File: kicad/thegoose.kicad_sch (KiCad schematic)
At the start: 35 parts, among them U1 DRV8848, U2 DRV8848, U3 DRV8848, U4 AP64500SP-13

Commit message: Tie DRV8848 sense pins to GND
AISEN and BISEN on U1-U3 were left open, so the H-bridges' low side had
no return path. Without current limiting, the data sheet says to tie
them to GND. Done in the SKiDL source, the schematic and the PCB (short
tracks from each pad to GND).

The PCB file is now saved in KiCad 10 format, which accounts for most of
its diff.

Co-Authored-By: Claude Opus 5.5 <noreply@anthropic.com>
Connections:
- net GND: now also U1.3 (AISEN), U1.6 (BISEN), U2.3 (AISEN), U2.6 (BISEN), U3.3 (AISEN), U3.6 (BISEN)
- no-connect marks 16 -> 10

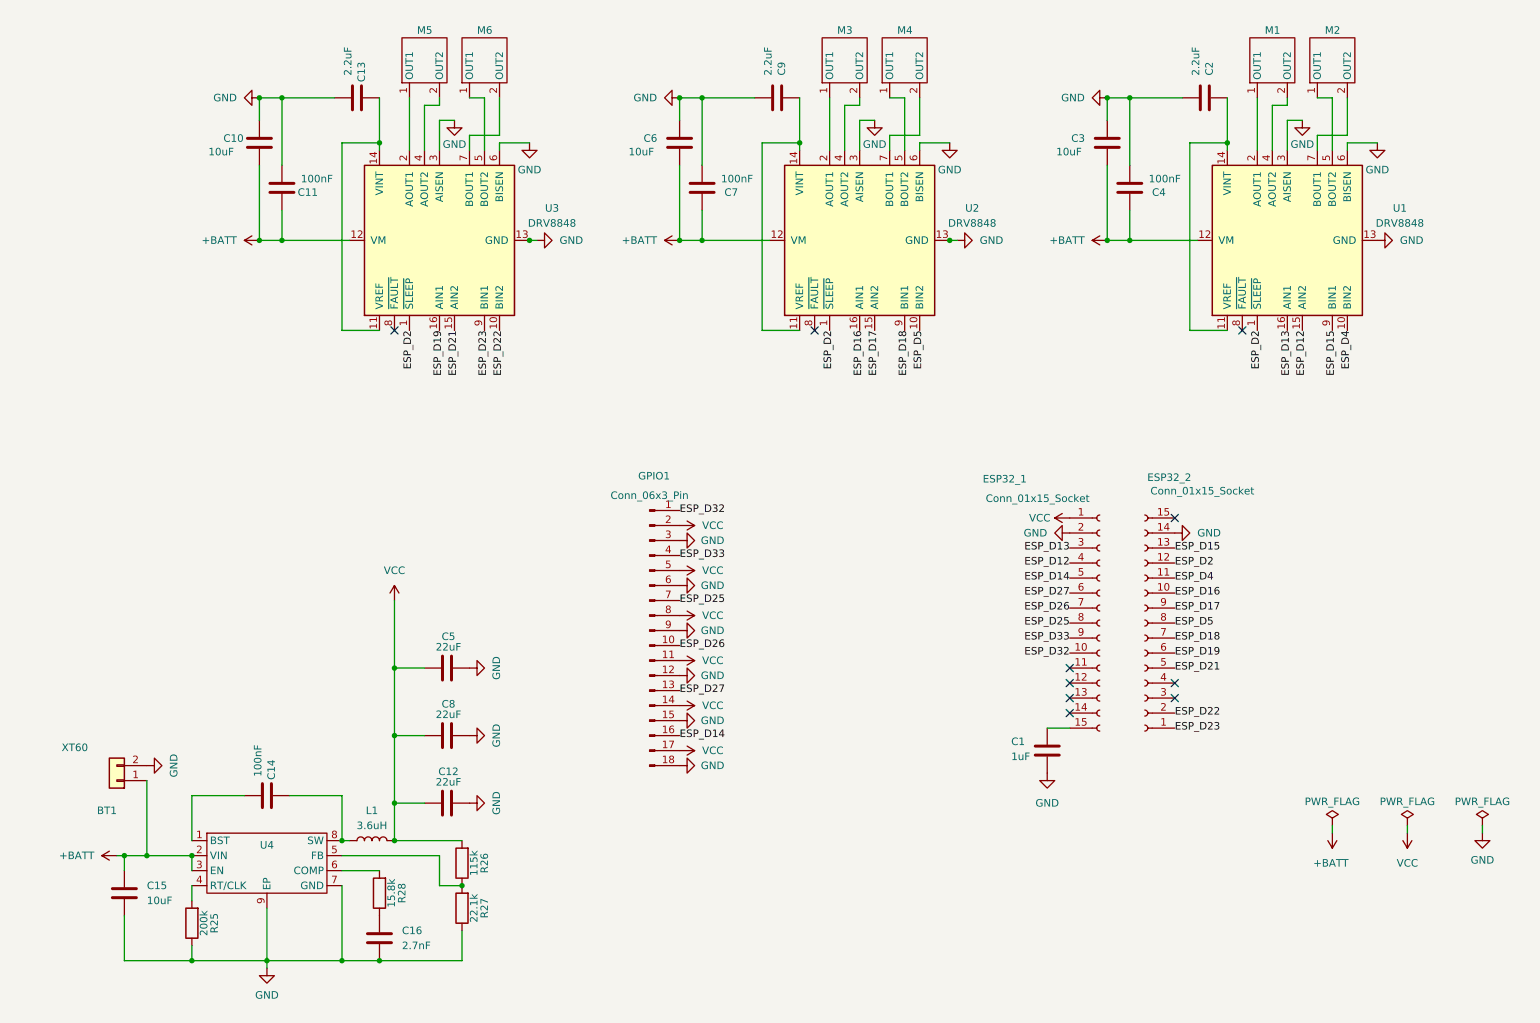
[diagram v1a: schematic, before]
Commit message: Tidy the schematic with the review loop
Six schematic-loop iterations raised the critic score from 2.9 to 4.3:
clearer power symbols, separated wiring, block titles and design notes.
Connectivity is unchanged (the netlist still matches SKiDL).

Co-Authored-By: Claude Opus 5.5 <noreply@anthropic.com>
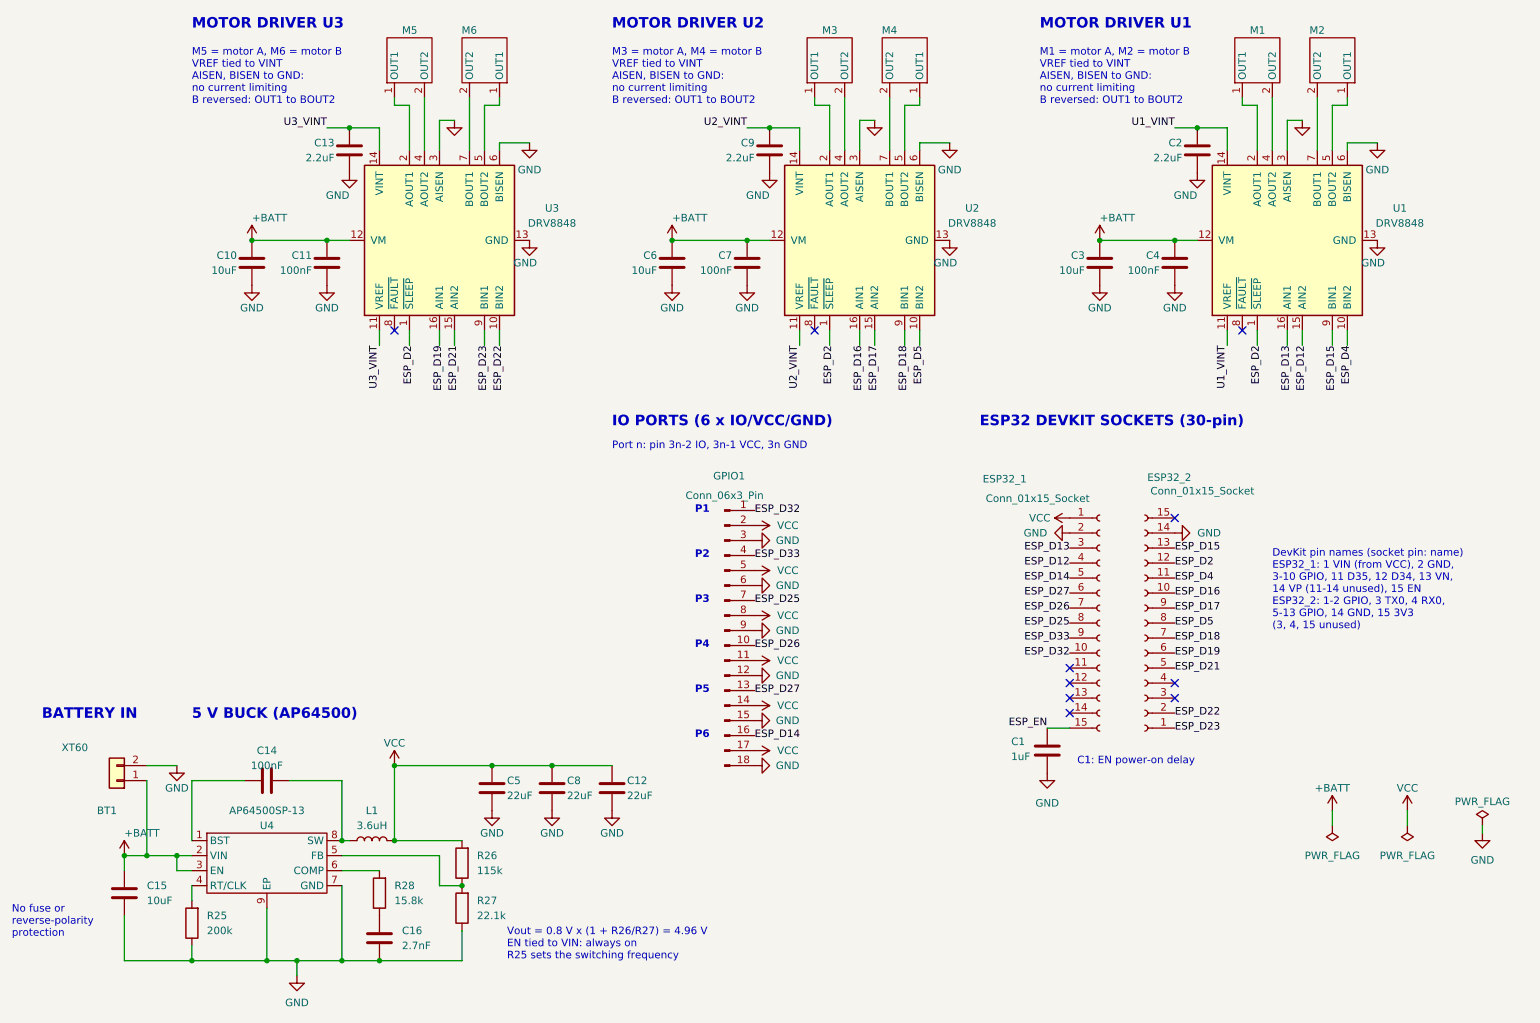
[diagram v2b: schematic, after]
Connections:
- net U1_VINT: now reaches C2.1, U1.11 (VREF), U1.14 (VINT)
- net ESP_EN: now reaches C1.1, ESP32_1.15 (Pin_15)
- net U3_VINT: now reaches C13.1, U3.11 (VREF), U3.14 (VINT)
- net U2_VINT: now reaches C9.1, U2.11 (VREF), U2.14 (VINT)
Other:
- note added: "5 V BUCK (AP64500)"
- note added: "BATTERY IN"
- note added: "C1: EN power-on delay"
- note added: "DevKit pin names (socket pin: name) ESP32_1: 1 VIN (from VCC), 2 GND, 3-10 GPIO, 11 D35, 12 D34, 13 VN, 14 VP (11-14 unused), 15 EN ESP32_2: 1-2 GPIO, 3 TX0, 4 RX0, 5-13 GPIO, 14 GND, 15 3V3 (3, 4, 15 unused)"
- note added: "ESP32 DEVKIT SOCKETS (30-pin)"
- note added: "IO PORTS (6 x IO/VCC/GND)"
- note added: "M1 = motor A, M2 = motor B VREF tied to VINT AISEN, BISEN to GND: no current limiting B reversed: OUT1 to BOUT2"
- note added: "M3 = motor A, M4 = motor B VREF tied to VINT AISEN, BISEN to GND: no current limiting B reversed: OUT1 to BOUT2"
- note added: "M5 = motor A, M6 = motor B VREF tied to VINT AISEN, BISEN to GND: no current limiting B reversed: OUT1 to BOUT2"
- note added: "MOTOR DRIVER U1"
- note added: "MOTOR DRIVER U2"
- note added: "MOTOR DRIVER U3"
- note added: "No fuse or reverse-polarity protection"
- note added: "P1"
- note added: "P2"
- note added: "P3"
- note added: "P4"
- note added: "P5"
- note added: "P6"
- note added: "Port n: pin 3n-2 IO, 3n-1 VCC, 3n GND"
- note added: "Vout = 0.8 V x (1 + R26/R27) = 4.96 V EN tied to VIN: always on R25 sets the switching frequency"
- moved on the sheet: C10, C11, C12, C13, C14, C2, C3, C4, C5, C6, C7, C8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

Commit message: Draw the rev 2 schematic as hierarchical sheets
Top sheet plus Power & charging, MCU & USB, Motor drivers and IO,
redrawn from circuit/goosebrain.py and tidied with the schematic loop.
ERC is clean and the netlist matches SKiDL, including MPN and LCSC.

- Add footprints for the Abracon AOTA core inductor and the Amphenol
  87520 USB-A receptacle.
- Fix L1's footprint name for KiCad 10's Wurth library.
- Keep battery sense on VSYS so it drains nothing with the switch off.
- Update the schematic critic's rubric for the rev 2 blocks.

Co-Authored-By: Claude Opus 5.5 <noreply@anthropic.com>
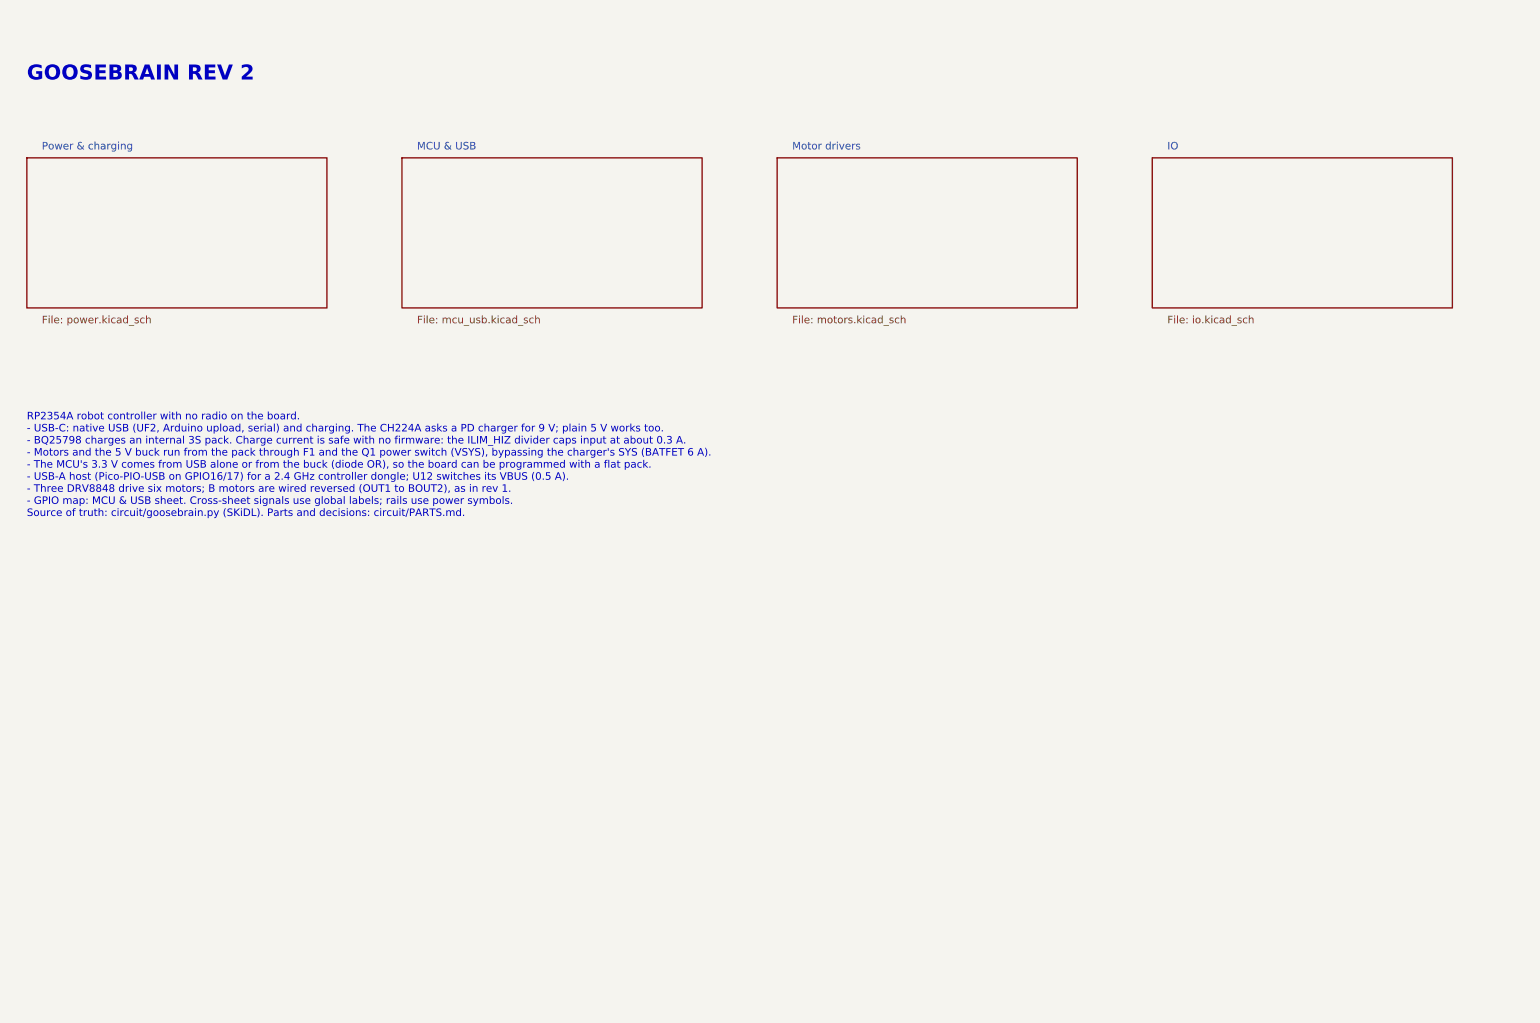
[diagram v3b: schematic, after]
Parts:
- removed BT1: XT60, hexy:AMASS_XT60PW-M_1x02_P7.20mm_Horizontal, symbol Connector_Generic:Conn_01x02
- removed C1: 1uF, Capacitor_SMD:C_0805_2012Metric, symbol Device:C
- removed C10, C15, C3, C6: 10uF, Capacitor_SMD:C_0805_2012Metric, symbol Device:C
- removed C11, C14, C4, C7: 100nF, Capacitor_SMD:C_0805_2012Metric, symbol Device:C
- removed C12, C5, C8: 22uF, Capacitor_SMD:C_0603_1608Metric, symbol Device:C
- removed C13, C2, C9: 2.2uF, Capacitor_SMD:C_0805_2012Metric, symbol Device:C
- removed C16: 2.7nF, Capacitor_SMD:C_0603_1608Metric, symbol Device:C
- removed ESP32_1, ESP32_2: Conn_01x15_Socket, Connector_PinSocket_2.54mm:PinSocket_1x15_P2.54mm_Vertical, symbol Connector:Conn_01x15_Socket
- removed GPIO1: Conn_06x3_Pin, hexy:PinHeader_3x06_P2.54mm_Horizontal, symbol Connector:Conn_01x18_Pin
- removed L1: 3.6uH, Inductor_SMD_Wurth:L_Wurth_WE-LQSH-4020, symbol Device:L
- removed M1, M2, M3, M4, M5, M6: ~, hexy:JST_XH_S2B-XH-A_1x02_P2.50mm_Horizontal, symbol hexyhustle:motor
- removed R25: 200k, Resistor_SMD:R_0805_2012Metric_Pad1.20x1.40mm_HandSolder, symbol Device:R
- removed R26: 115k, Resistor_SMD:R_0805_2012Metric_Pad1.20x1.40mm_HandSolder, symbol Device:R
- removed R27: 22.1k, Resistor_SMD:R_0805_2012Metric_Pad1.20x1.40mm_HandSolder, symbol Device:R
- removed R28: 15.8k, Resistor_SMD:R_0805_2012Metric_Pad1.20x1.40mm_HandSolder, symbol Device:R
- removed U1, U2, U3: DRV8848, Package_SO:TSSOP-16-1EP_4.4x5mm_P0.65mm, symbol Driver_Motor:DRV8848
- removed U4: AP64500SP-13, Package_SO:Diodes_SO-8EP, symbol hexyhustle:AP64500-13
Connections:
- no-connect marks 10 -> 0
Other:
- added sheet IO (io.kicad_sch)
- added sheet MCU & USB (mcu_usb.kicad_sch)
- added sheet Motor drivers (motors.kicad_sch)
- added sheet Power & charging (power.kicad_sch)
- note added: "GOOSEBRAIN REV 2"
- note added: "RP2354A robot controller with no radio on the board. - USB-C: native USB (UF2, Arduino upload, serial) and charging. The CH224A asks a PD charger for 9 V; plain 5 V works too. - BQ25798 charges an internal 3S pack. Charge current is safe with no firmware: the ILIM_HIZ divider caps input at about 0.3 A. - Motors and the 5 V buck run from the pack through F1 and the Q1 power switch (VSYS), bypassin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"
- note removed: "5 V BUCK (AP64500)"
- note removed: "BATTERY IN"
- note removed: "C1: EN power-on delay"
- note removed: "DevKit pin names (socket pin: name) ESP32_1: 1 VIN (from VCC), 2 GND, 3-10 GPIO, 11 D35, 12 D34, 13 VN, 14 VP (11-14 unused), 15 EN ESP32_2: 1-2 GPIO, 3 TX0, 4 RX0, 5-13 GPIO, 14 GND, 15 3V3 (3, 4, 15 unused)"
- note removed: "ESP32 DEVKIT SOCKETS (30-pin)"
- note removed: "IO PORTS (6 x IO/VCC/GND)"
- note removed: "M1 = motor A, M2 = motor B VREF tied to VINT AISEN, BISEN to GND: no current limiting B reversed: OUT1 to BOUT2"
- note removed: "M3 = motor A, M4 = motor B VREF tied to VINT AISEN, BISEN to GND: no current limiting B reversed: OUT1 to BOUT2"
- note removed: "M5 = motor A, M6 = motor B VREF tied to VINT AISEN, BISEN to GND: no current limiting B reversed: OUT1 to BOUT2"
- note removed: "MOTOR DRIVER U1"
- note removed: "MOTOR DRIVER U2"
- note removed: "MOTOR DRIVER U3"
- note removed: "No fuse or reverse-polarity protection"
- note removed: "P1"
- note removed: "P2"
- note removed: "P3"
- note removed: "P4"
- note removed: "P5"
- note removed: "P6"
- note removed: "Port n: pin 3n-2 IO, 3n-1 VCC, 3n GND"
- note removed: "Vout = 0.8 V x (1 + R26/R27) = 4.96 V EN tied to VIN: always on R25 sets the switching frequency"

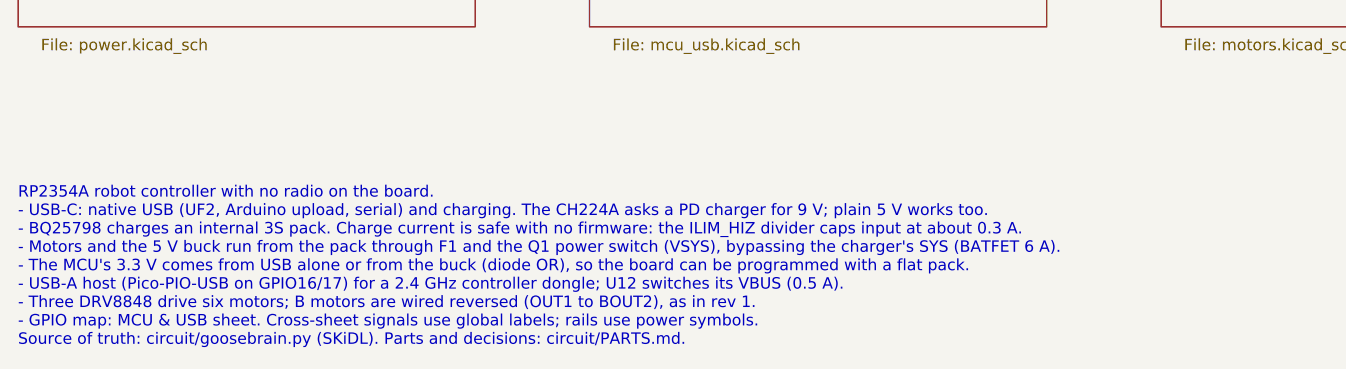
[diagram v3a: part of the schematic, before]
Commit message: Re-lay out rev 2 around an Ovonic 450 pack on top of the board
The internal pack is now an Ovonic 3S 450 mAh XT30 pack sitting 2 mm
above the board over the low-power logic area, on an XT30 pigtail. The
board is 88.5 x 47 mm with 2 mm corner radii, for a box of about
93.5 x 52 x 24.6 mm whose face has no openings.

- IO S1-S6 are a 3 x 6 right-angle header out of the left end, beside
  M5/M6, replacing the recessed vertical block.
- BOOT is a side-push switch on the top edge behind a pinhole sized for
  a 2.5 mm hex key; RESET is removed, with RUN on a bottom test pad
  beside SWCLK/SWDIO/GND.
- The CHG LED is a side-view part on the top edge; the GPIO status LED
  is removed now that the WS2812B stick shows status.
- The pack NTC is removed (a fixed 10k holds the charger's TS at 25 C);
  the protector's on-board TH1 stays.
- Q1, F1 and the other warm parts moved out from under the pack, and the
  GPIO map was re-swapped for the new placement (I2C on I2C1).

Schematic review passes; PCB review passes every gate except unrouted.

Co-Authored-By: Claude Opus 5.5 <noreply@anthropic.com>
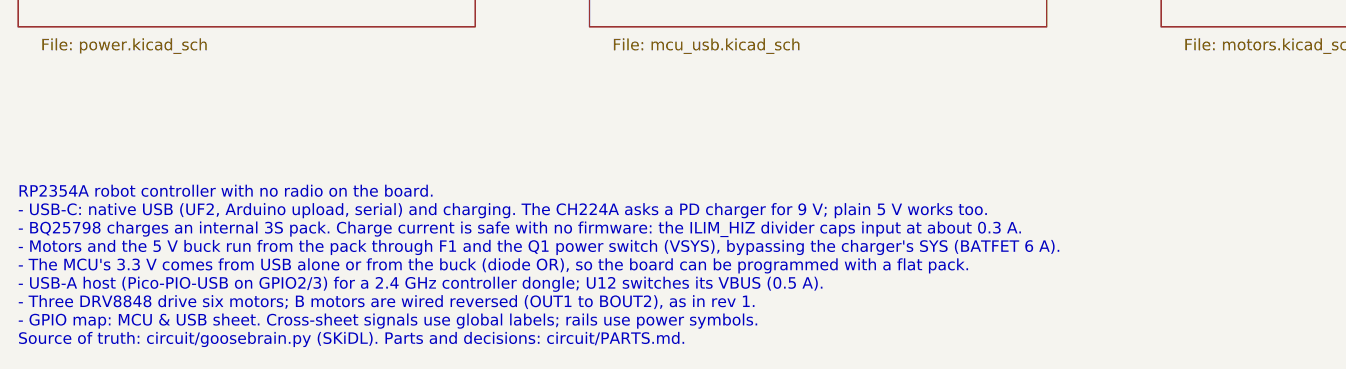
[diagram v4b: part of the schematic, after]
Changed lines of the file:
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@@
 		)
 	)
-	(text "RP2354A robot controller with no radio on the board.\n- USB-C: native USB (UF2, Arduino upload, serial) and charging. The CH224A asks a PD charger for 9 V; plain 5 V works too.\n- BQ25798 charges an internal 3S pack. Charge current is safe with no firmware: the ILIM_HIZ divider caps input at about 0.3 A.\n- Motors and the 5 V buck run from the pack through F1 and the Q1 power switch (VSYS), bypassing the charger's SYS (BATFET 6 A).\n- The MCU's 3.3 V comes from USB alone or from the buck (diode OR), so the board can be programmed with a flat pack.\n- USB-A host (Pico-PIO-USB on GPIO16/17) for a 2.4 GHz controller dongle; U12 switches its VBUS (0.5 A).\n- Three DRV8848 drive six motors; B motors are wired reversed (OUT1 to BOUT2), as in rev 1.\n- GPIO map: MCU & USB sheet. Cross-sheet signals use global labels; rails use power symbols.\nSource of truth: circuit/goosebrain.py (SKiDL). Parts and decisions: circuit/PARTS.md."
+	(text "RP2354A robot controller with no radio on the board.\n- USB-C: native USB (UF2, Arduino upload, serial) and charging. The CH224A asks a PD charger for 9 V; plain 5 V works too.\n- BQ25798 charges an internal 3S pack. Charge current is safe with no firmware: the ILIM_HIZ divider caps input at about 0.3 A.\n- Motors and the 5 V buck run from the pack through F1 and the Q1 power switch (VSYS), bypassing the charger's SYS (BATFET 6 A).\n- The MCU's 3.3 V comes from USB alone or from the buck (diode OR), so the board can be programmed with a flat pack.\n- USB-A host (Pico-PIO-USB on GPIO2/3) for a 2.4 GHz controller dongle; U12 switches its VBUS (0.5 A).\n- Three DRV8848 drive six motors; B motors are wired reversed (OUT1 to BOUT2), as in rev 1.\n- GPIO map: MCU & USB sheet. Cross-sheet signals use global labels; rails use power symbols.\nSource of truth: circuit/goosebrain.py (SKiDL). Parts and decisions: circuit/PARTS.md."
 		(exclude_from_sim no)
 		(at 25.4 81.28 0)
